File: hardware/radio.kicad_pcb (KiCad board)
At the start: 2 copper layers, 100 x 50 mm, 62 parts, among them J1 105450-0101, J2 Conn_01x02, J3 Conn_01x02, J4 Conn_01x04, J5 Conn_01x02_Male, Q1 Q_PMOS_DGS, Q2 Q_NMOS_DGS, Q3 Q_NMOS_DGS, Q4 Q_PMOS_DGS, SW1 SW_BOOT, SW2 SW_RST, SW3 SW_1, SW4 Rot_Enc, SW5 SW_2, SW6 SW_3, U1 TP4056, U2 ESP32-WROOM-32, U3 TPS5432, U4 MAX98357

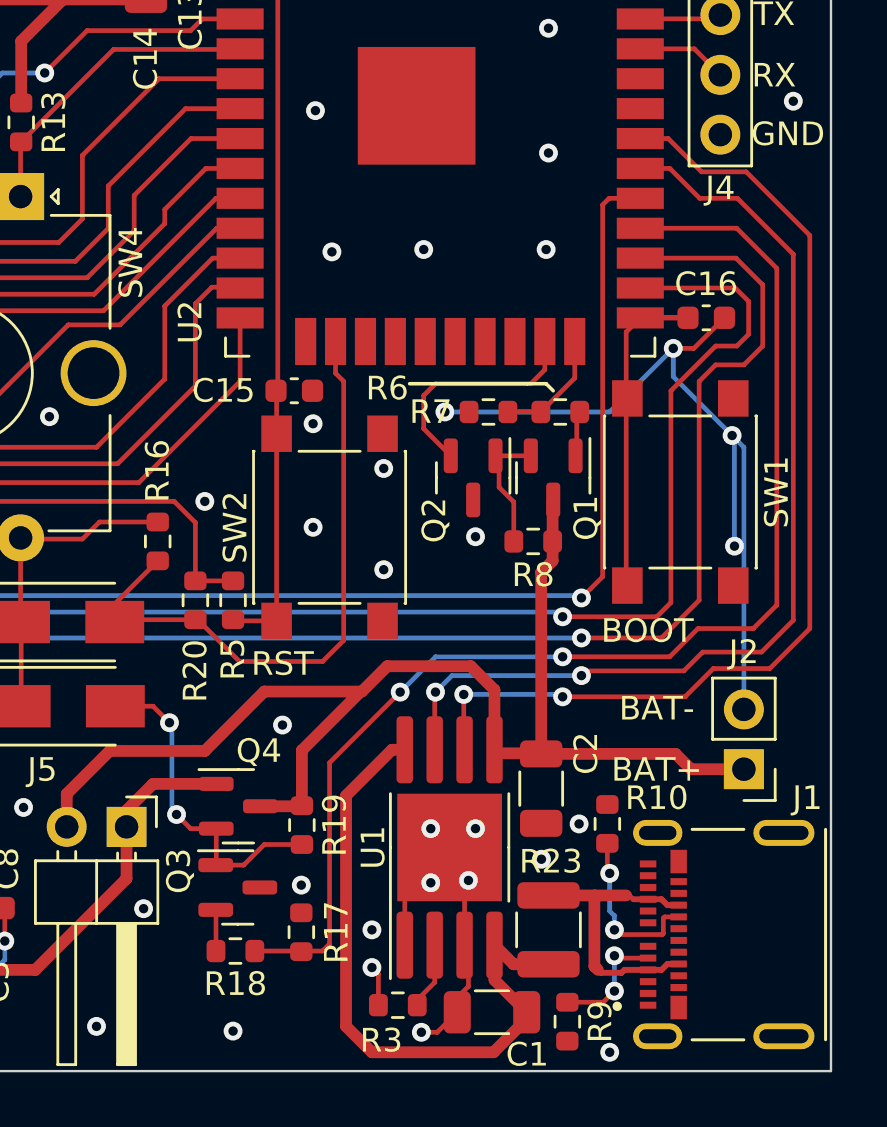
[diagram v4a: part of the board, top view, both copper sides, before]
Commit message: added 'Current measurement' and 'UART' labels to J5 and J4 respectively
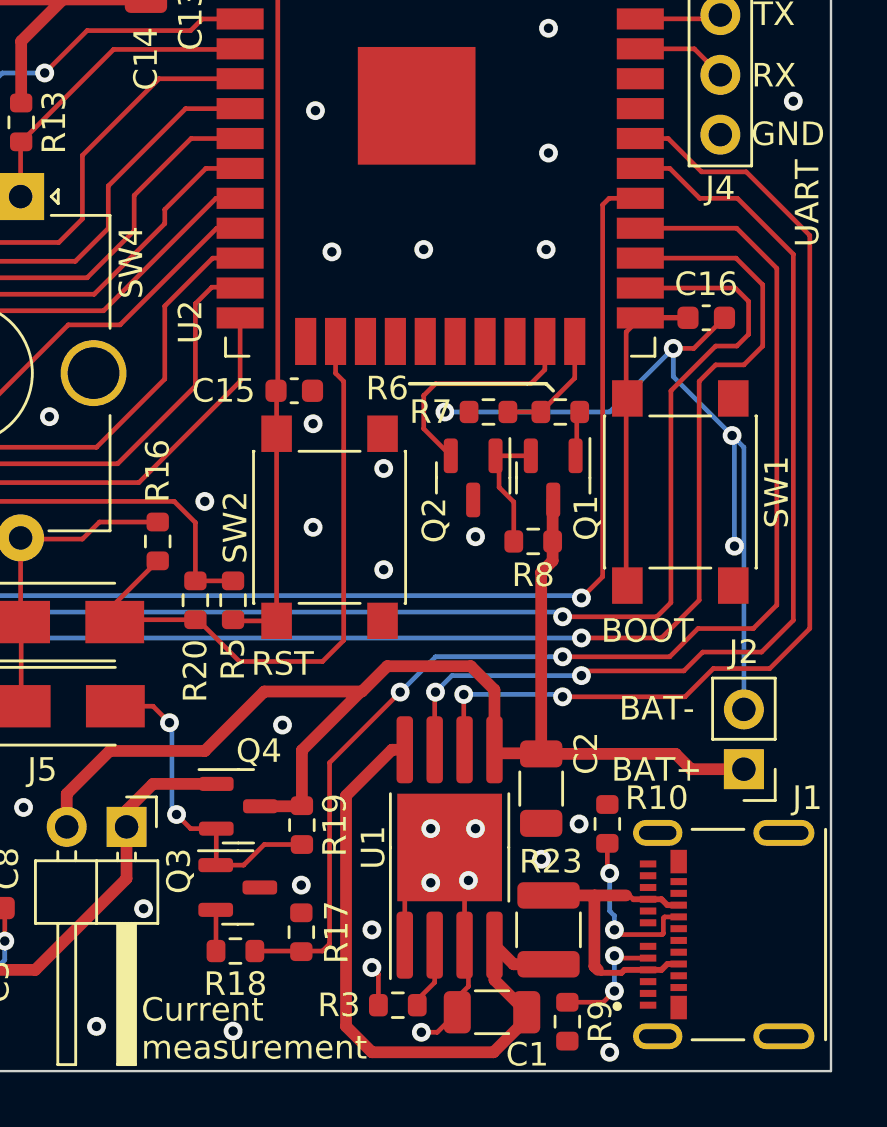
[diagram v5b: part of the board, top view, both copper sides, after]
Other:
- board text added: "Current measurement"
- board text added: "UART"
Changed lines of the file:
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@@
     (property "Sheetname" "")
     (attr smd)
-    (fp_text reference "R3" (at 0.7 -1.5) (layer "F.SilkS")
+    (fp_text reference "R3" (at 2.5 0) (layer "F.SilkS")
       (effects (font (size 1 1) (thickness 0.15)))
     )
@@
     (effects (font (size 1 1) (thickness 0.15)) (justify left))
   )
+  (gr_text "UART\n" (at 129 45 90) (layer "F.SilkS")
+    (effects (font (size 1 1) (thickness 0.15)) (justify left))
+  )
   (gr_text "-\n" (at 31.1 55.6) (layer "F.SilkS")
     (effects (font (size 1 1) (thickness 0.15)))
@@
     (effects (font (size 1 1) (thickness 0.15)))
   )
+  (gr_text "Current\nmeasurement\n" (at 100.7 78.2) (layer "F.SilkS")
+    (effects (font (size 1 1) (thickness 0.15)) (justify left))
+  )
   (segment (start 101.455 37.845) (end 104.9 37.845) (width 0.2) (layer "F.Cu") (net 1))

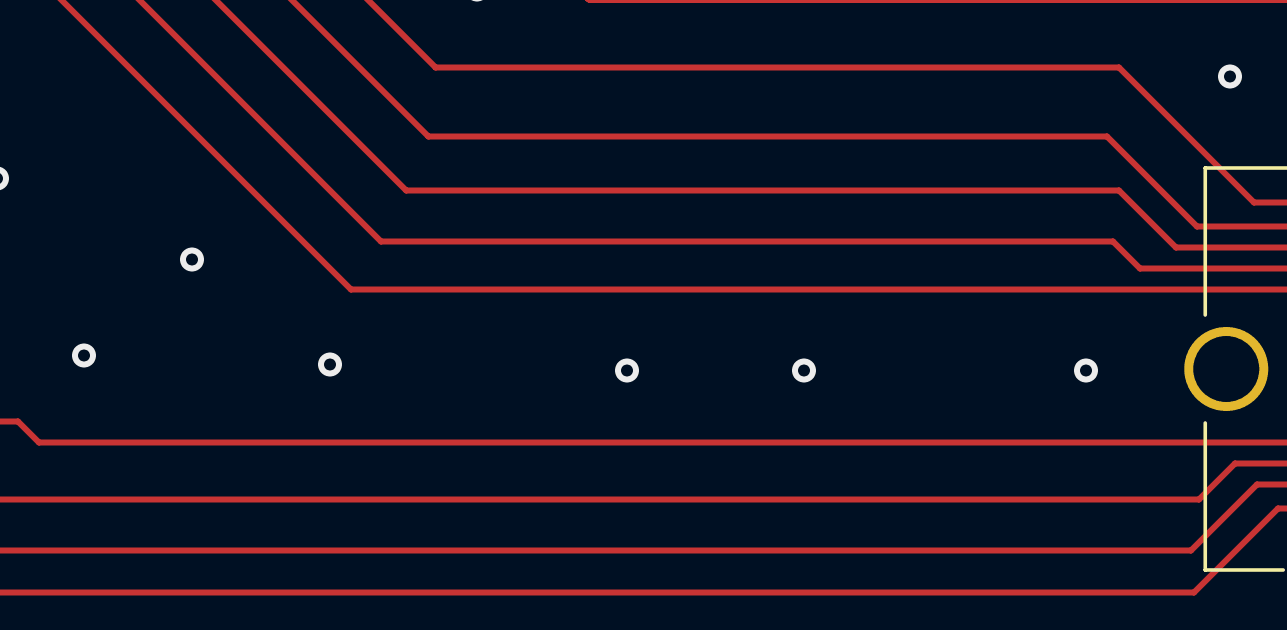
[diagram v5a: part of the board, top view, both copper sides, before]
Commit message: Added project description to bottom silkscreen
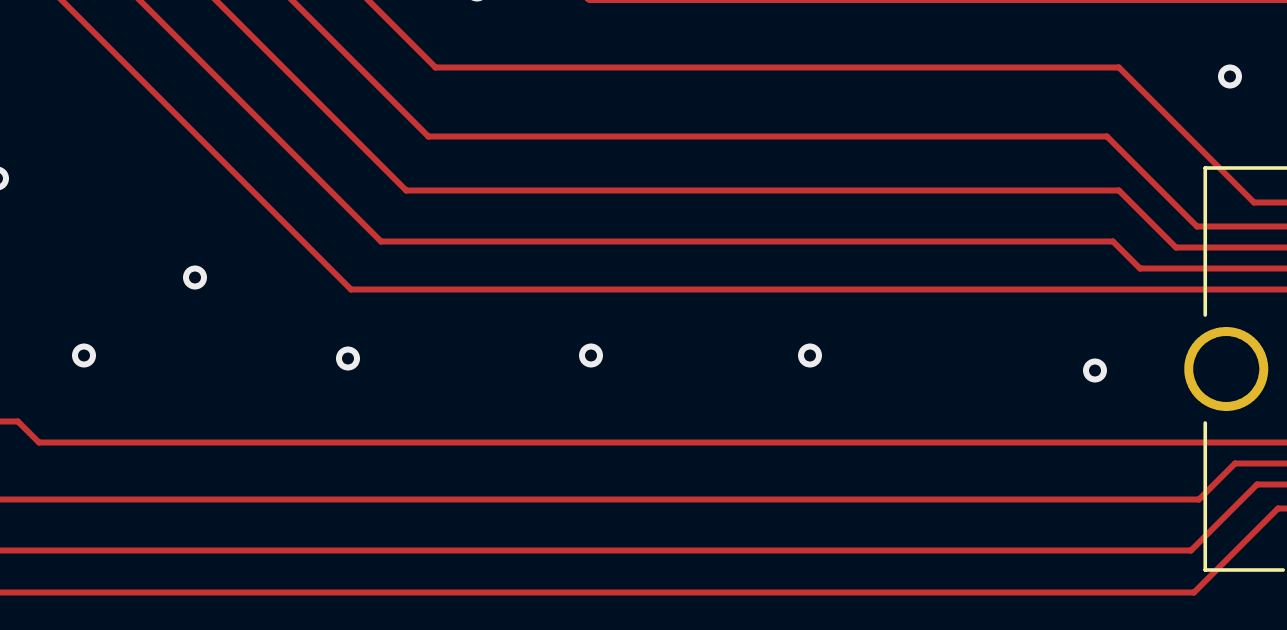
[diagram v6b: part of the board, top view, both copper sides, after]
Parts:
- added G***: LOGO, LOGO, B.Cu at (65.6, 42.8)
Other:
- board text added: "Projekt badawczy 2022/2023"
- board text added: "Radio internetowe o niskim poborze mocy"

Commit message: redone DC-DC converter layout to match the reference in datasheet
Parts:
- added TP1: TestPoint, TestPoint:TestPoint_Loop_D2.50mm_Drill1.0mm, F.Cu at (33.5, 76.7)
- added TP2: TestPoint, TestPoint:TestPoint_Loop_D2.50mm_Drill1.0mm, F.Cu at (80.3, 67.8)
- L1: footprint wyswietlacze:L_2010Metric -> wyswietlacze:DJNR6028-2R2-S
- moved R2 7.38 mm to (75.9, 71.4), turned to 180 degrees
- moved C4 5.90 mm to (85.7, 78.7), turned to 180 degrees
- moved R1 5.35 mm to (78.2, 70.6), turned to -90 degrees
- moved C3 4.69 mm to (88.4, 74.4), turned to 90 degrees
- moved C5 4.23 mm to (75.9, 72.9)
- moved C6 3.94 mm to (76.7, 76.7)
- moved R4 3.44 mm to (77.5, 74.4)
- moved C8 3.25 mm to (93.2, 76.2), turned to 180 degrees
- moved U3 2.80 mm to (83.1, 75.2)
- moved C7 2.65 mm to (78.2, 78.0), turned to -90 degrees
- moved L1 1.36 mm to (92.7, 71.9)
- moved C11 0.99 mm to (87.1, 69.8)
- moved C12 0.90 mm to (87.1, 67.5)
- moved J5 0.25 mm to (100.3, 69.6)
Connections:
- J1 pad S1: unconnected-(J1-PadS1) -> (no net)
- J1 pad S2: unconnected-(J1-PadS1) -> (no net)
- J1 pad S3: unconnected-(J1-PadS1) -> (no net)
- J1 pad S4: unconnected-(J1-PadS1) -> (no net)
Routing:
- net Net-(C3-Pad1): track 20.8 -> 31.3 mm
- net GND: track 62.2 -> 68.9 mm, vias 97 -> 83
- net Net-(C8-Pad1): track 5.08 -> 9.50 mm
- net +3V3: track 257.9 -> 262.4 mm
- net Net-(C8-Pad2): track 11.0 -> 7.08 mm
- net BTN_3: track 88.5 -> 90.0 mm
- net Net-(C5-Pad1): track 3.59 -> 4.80 mm
- net Net-(R1-Pad2): track 3.66 -> 4.30 mm
- added copper zone on F.Cu, net +3V3
- added copper zone on F.Cu, net Net-(C8-Pad1)

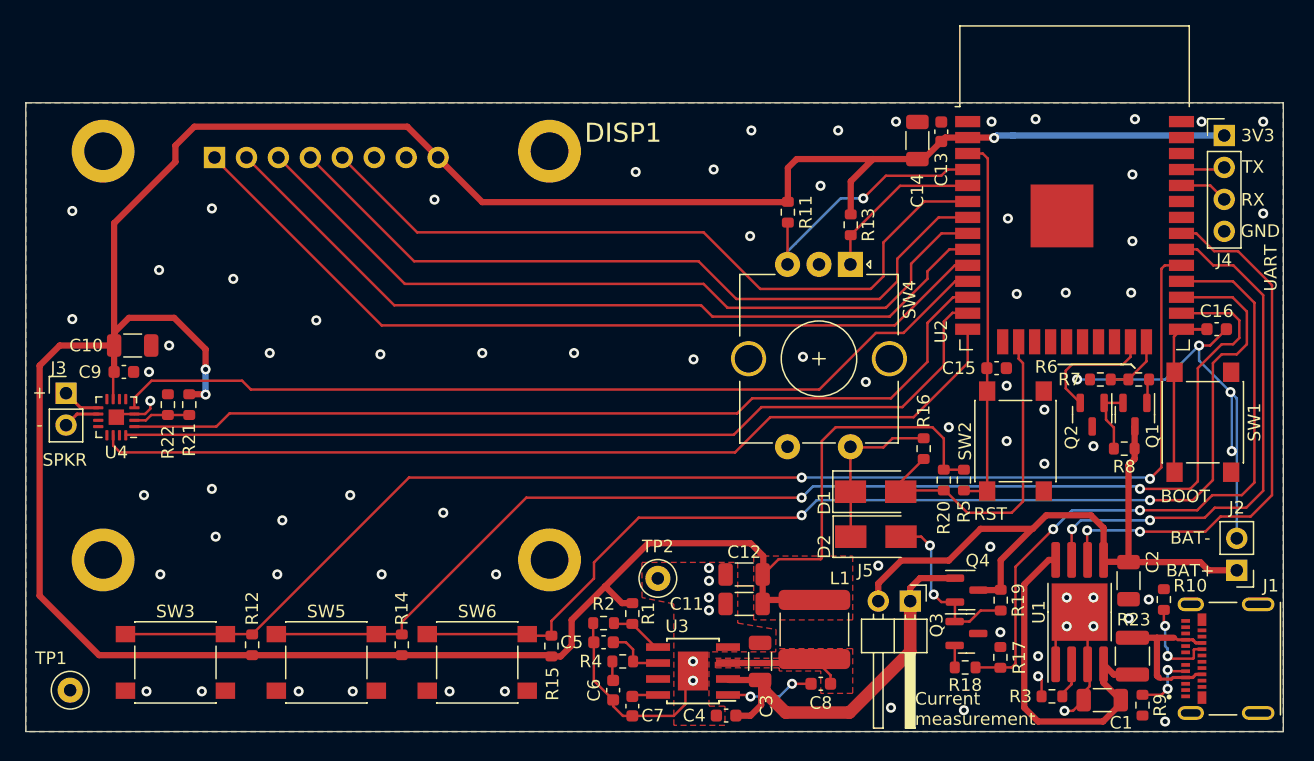
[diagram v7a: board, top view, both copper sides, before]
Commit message: removed copper pour on signal layer because Eric Bogatin said so
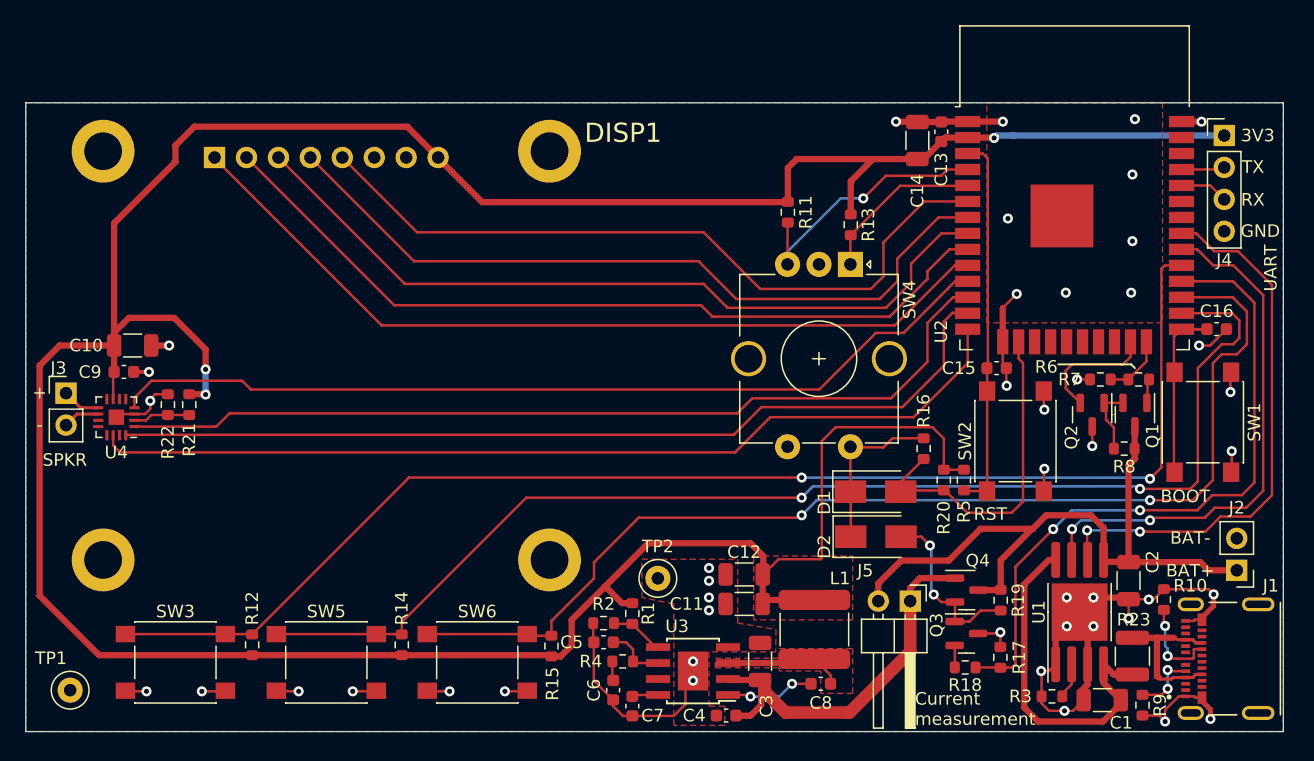
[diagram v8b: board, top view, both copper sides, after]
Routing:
- net GND: track 68.9 -> 111.8 mm, vias 83 -> 45
